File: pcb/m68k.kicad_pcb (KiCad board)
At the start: 2 copper layers, 100 x 100 mm, 120 parts, among them J1 USB_B_Micro, J2 Mini-DIN-6, J4 DB15_Male_HighDensity, J5 FTSH-105-01-L-DV-K, J6 FTSH-105-01-L-DV-K, J7 FTSH-105-01-L-DV-K, J8 Micro_SD_Card, U1 93LC56, U10 25LCxxx, U11 TXB0108DQSR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

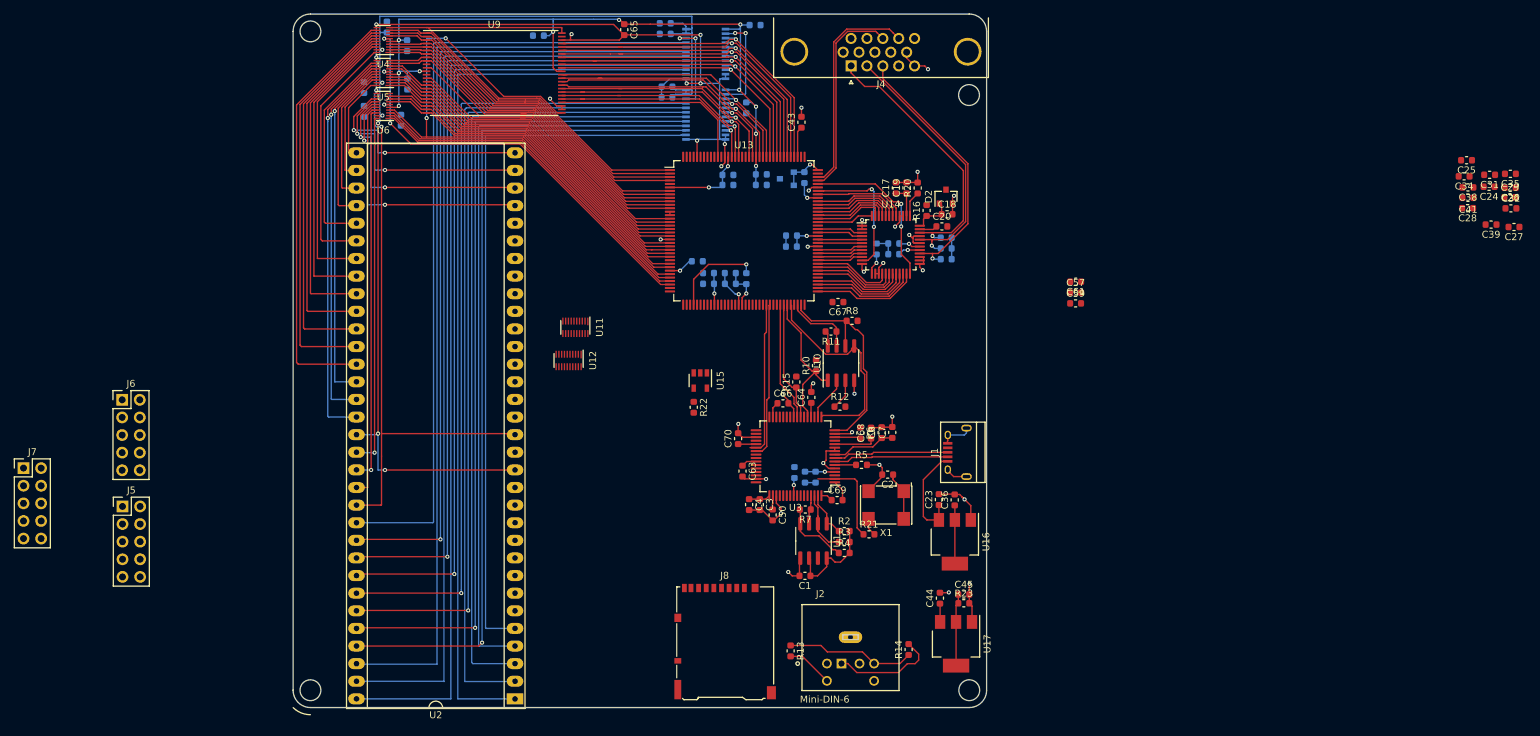
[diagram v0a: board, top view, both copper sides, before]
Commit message: Cleaned up CAPS
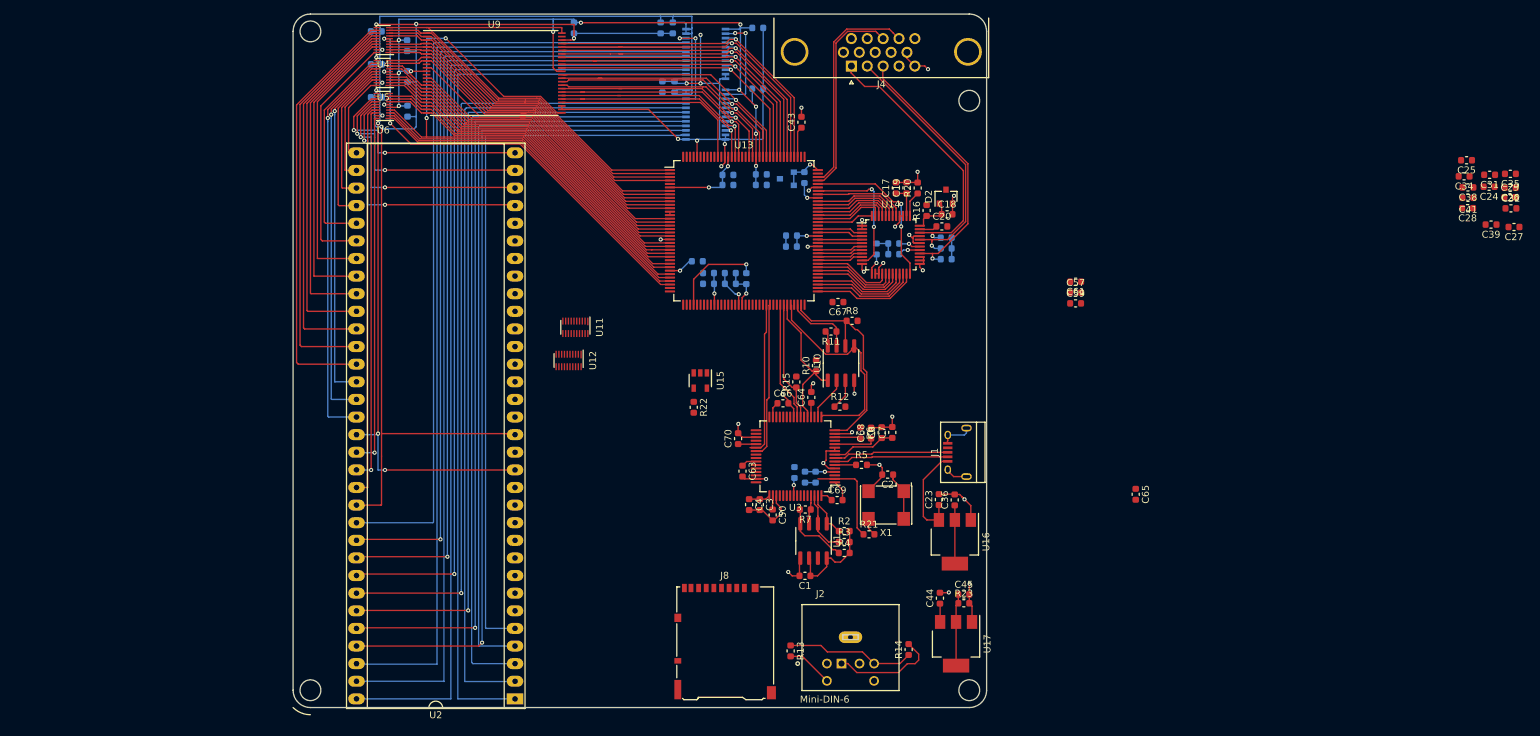
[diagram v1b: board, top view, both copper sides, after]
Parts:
- removed J5, J6, J7: FTSH-105-01-L-DV-K, Connector_PinHeader_2.54mm:PinHeader_2x05_P2.54mm_Vertical
- moved C65 99.6 mm to (141.5, 89.2)
- moved C54 5.25 mm to (60.5, 22.0), turned to 270 degrees
- moved C49 3.79 mm to (32.0, 27.2), turned to 180 degrees
- moved C60 3.23 mm to (87.0, 30.8), turned to 0 degrees
- moved C55 2.70 mm to (32.0, 32.0), turned to 180 degrees
- moved C42 1.65 mm to (32.0, 22.5), turned to 180 degrees
- moved C53 1.64 mm to (73.2, 30.5), turned to 90 degrees
- moved C52 1.61 mm to (36.5, 34.0)
- moved C46 1.39 mm to (74.8, 22.0), turned to 270 degrees
- moved C16 1.10 mm to (36.5, 29.0)
- moved C51 1.09 mm to (75.0, 30.5), turned to 90 degrees
- moved C47 0.94 mm to (73.0, 22.0), turned to 270 degrees
- moved C56 0.56 mm to (87.0, 22.0)
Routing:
- net GND: track 312.1 -> 367.0 mm, vias 38 -> 39
- net +5V: track 196.5 -> 199.8 mm
- net +3V3: track 217.8 -> 218.4 mm
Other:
- outline, holes or cut-outs redrawn

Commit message: Repin
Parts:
- moved U11 13.5 mm to (59.5, 51.8), turned to 180 degrees
- moved U12 12.3 mm to (59.9, 57.6), turned to 180 degrees
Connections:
- U13 pad 107: DIR -> BERRn
- U13 pad 110: BERRn -> DIR
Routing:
- net DIR: track 14.6 -> 26.3 mm, vias 2 -> 3
- net GND: track 367.0 -> 375.1 mm
- net +3V3: track 218.4 -> 217.0 mm

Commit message: SRAM!!!!
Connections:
- U13 pad 135: Net-(U11-Pad4) -> DATA_OEn
- U13 pad 136: Net-(U11-Pad7) -> Net-(U11-Pad4)
- U13 pad 137: Net-(U11-Pad8) -> Net-(U11-Pad7)
- U13 pad 138: Net-(U12-Pad1) -> Net-(U11-Pad8)
- U13 pad 139: Net-(U12-Pad2) -> Net-(U12-Pad1)
- U13 pad 141: Net-(U12-Pad3) -> Net-(U12-Pad2)
- U13 pad 142: Net-(U12-Pad4) -> Net-(U12-Pad3)
- U13 pad 143: Net-(U12-Pad7) -> Net-(U12-Pad4)
- U13 pad 144: Net-(U13-Pad144) -> /CE#
- U13 pad 60: DATA_OEn -> Net-(U12-Pad7)
- U9 pad 26: GND -> /CE#
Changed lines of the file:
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@@
   (net 241 "Net-(J2-Pad2)")
   (net 242 "Net-(U13-Pad134)")
-  (net 243 "Net-(U13-Pad144)")
-  (net 244 ADBUS)
+  (net 243 ADBUS)
+  (net 244 /CE#)
   (net_class Default "This is the default net class."
     (clearance 0.127)
@@
     (add_net /A8)
     (add_net /A9)
+    (add_net /CE#)
     (add_net /D0)
     (add_net /D1)
@@
     (add_net "Net-(U13-Pad133)")
     (add_net "Net-(U13-Pad134)")
-    (add_net "Net-(U13-Pad144)")
     (add_net "Net-(U13-Pad35)")
     (add_net "Net-(U13-Pad36)")
@@
       (net 1 GND))
     (pad 60 smd roundrect (at 2.75 10.6625) (size 0.3 1.475) (layers F.Cu F.Paste F.Mask) (roundrect_rratio 0.25)
-      (net 130 DATA_OEn))
+      (net 148 "Net-(U12-Pad7)"))
     (pad 61 smd roundrect (at 3.25 10.6625) (size 0.3 1.475) (layers F.Cu F.Paste F.Mask) (roundrect_rratio 0.25)
       (net 94 RX))
@@
       (net 26 nWP))
     (pad 64 smd roundrect (at 4.75 10.6625) (size 0.3 1.475) (layers F.Cu F.Paste F.Mask) (roundrect_rratio 0.25)
-      (net 244 ADBUS))
+      (net 243 ADBUS))
     (pad 65 smd roundrect (at 5.25 10.6625) (size 0.3 1.475) (layers F.Cu F.Paste F.Mask) (roundrect_rratio 0.25)
       (net 95 CDONE))
@@
       (net 242 "Net-(U13-Pad134)"))
     (pad 135 smd roundrect (at -4.25 -10.6625) (size 0.3 1.475) (layers F.Cu F.Paste F.Mask) (roundrect_rratio 0.25)
-      (net 144 "Net-(U11-Pad4)"))
+      (net 130 DATA_OEn))
     (pad 136 smd roundrect (at -4.75 -10.6625) (size 0.3 1.475) (layers F.Cu F.Paste F.Mask) (roundrect_rratio 0.25)
-      (net 143 "Net-(U11-Pad7)"))
+      (net 144 "Net-(U11-Pad4)"))
     (pad 137 smd roundrect (at -5.25 -10.6625) (size 0.3 1.475) (layers F.Cu F.Paste F.Mask) (roundrect_rratio 0.25)
-      (net 142 "Net-(U11-Pad8)"))
+      (net 143 "Net-(U11-Pad7)"))
     (pad 138 smd roundrect (at -5.75 -10.6625) (size 0.3 1.475) (layers F.Cu F.Paste F.Mask) (roundrect_rratio 0.25)
-      (net 145 "Net-(U12-Pad1)"))
+      (net 142 "Net-(U11-Pad8)"))
     (pad 139 smd roundrect (at -6.25 -10.6625) (size 0.3 1.475) (layers F.Cu F.Paste F.Mask) (roundrect_rratio 0.25)
-      (net 146 "Net-(U12-Pad2)"))
+      (net 145 "Net-(U12-Pad1)"))
     (pad 140 smd roundrect (at -6.75 -10.6625) (size 0.3 1.475) (layers F.Cu F.Paste F.Mask) (roundrect_rratio 0.25)
       (net 1 GND))
     (pad 141 smd roundrect (at -7.25 -10.6625) (size 0.3 1.475) (layers F.Cu F.Paste F.Mask) (roundrect_rratio 0.25)
-      (net 147 "Net-(U12-Pad3)"))
+      (net 146 "Net-(U12-Pad2)"))
     (pad 142 smd roundrect (at -7.75 -10.6625) (size 0.3 1.475) (layers F.Cu F.Paste F.Mask) (roundrect_rratio 0.25)
-      (net 179 "Net-(U12-Pad4)"))
+      (net 147 "Net-(U12-Pad3)"))
     (pad 143 smd roundrect (at -8.25 -10.6625) (size 0.3 1.475) (layers F.Cu F.Paste F.Mask) (roundrect_rratio 0.25)
-      (net 148 "Net-(U12-Pad7)"))
+      (net 179 "Net-(U12-Pad4)"))
     (pad 144 smd roundrect (at -8.75 -10.6625) (size 0.3 1.475) (layers F.Cu F.Paste F.Mask) (roundrect_rratio 0.25)
-      (net 243 "Net-(U13-Pad144)"))
+      (net 244 /CE#))
     (model ${KISYS3DMOD}/Package_QFP.3dshapes/TQFP-144_20x20mm_P0.5mm.wrl
       (at (xyz 0 0 0))
@@
       (net 96 "Net-(U10-Pad5)"))
     (pad 18 smd roundrect (at -3.25 5.675 180) (size 0.3 1.55) (layers F.Cu F.Paste F.Mask) (roundrect_rratio 0.25)
-      (net 244 ADBUS))
+      (net 243 ADBUS))
     (pad 19 smd roundrect (at -2.75 5.675 180) (size 0.3 1.55) (layers F.Cu F.Paste F.Mask) (roundrect_rratio 0.25)
       (net 197 "Net-(U3-Pad19)"))
@@
       (net 1 GND))
     (pad 26 smd rect (at 9.75 5.25) (size 1.1 0.25) (layers F.Cu F.Paste F.Mask)
-      (net 1 GND))
+      (net 244 /CE#))
     (pad 24 smd rect (at -9.75 5.75) (size 1.1 0.25) (layers F.Cu F.Paste F.Mask)
       (net 98 /a2))
@@
       (net 26 nWP))
     (pad 2 smd roundrect (at -2.475 -0.635 90) (size 1.95 0.6) (layers F.Cu F.Paste F.Mask) (roundrect_rratio 0.25)
-      (net 244 ADBUS))
+      (net 243 ADBUS))
     (pad 1 smd roundrect (at -2.475 -1.905 90) (size 1.95 0.6) (layers F.Cu F.Paste F.Mask) (roundrect_rratio 0.25)
       (net 24 "Net-(R10-Pad1)"))
@@
   (segment (start 81.25 35.266275) (end 81.25 40.5875) (width 0.127) (layer F.Cu) (net 242))
   (segment (start 78.733725 32.75) (end 81.25 35.266275) (width 0.127) (layer F.Cu) (net 242))
-  (segment (start 95.68 77.433674) (end 95.6862 77.427474) (width 0.2) (layer F.Cu) (net 244))
-  (segment (start 95.68 78.0976) (end 95.68 77.433674) (width 0.2) (layer F.Cu) (net 244))
-  (segment (start 95.6862 77.427474) (end 95.6862 76.74) (width 0.2) (layer F.Cu) (net 244))
-  (segment (start 98.3659 74.0603) (end 98.3659 72.8142) (width 0.2) (layer F.Cu) (net 244))
-  (segment (start 95.6862 76.74) (end 98.3659 74.0603) (width 0.2) (layer F.Cu) (net 244))
+  (segment (start 95.68 77.433674) (end 95.6862 77.427474) (width 0.2) (layer F.Cu) (net 243))
+  (segment (start 95.68 78.0976) (end 95.68 77.433674) (width 0.2) (layer F.Cu) (net 243))
+  (segment (start 95.6862 77.427474) (end 95.6862 76.74) (width 0.2) (layer F.Cu) (net 243))
+  (segment (start 98.3659 74.0603) (end 98.3659 72.8142) (width 0.2) (layer F.Cu) (net 243))
+  (segment (start 95.6862 76.74) (end 98.3659 74.0603) (width 0.2) (layer F.Cu) (net 243))
 )

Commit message: SRAM????
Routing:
- net +5V: track 199.8 -> 232.3 mm
- net /CE#: track 0.00 -> 21.0 mm
- net GND: track 375.1 -> 393.1 mm
- net DATA_OEn: track 13.3 -> 22.8 mm, vias 2 -> 3
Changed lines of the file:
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@@
     (thickness 1.6)
     (drawings 13)
-    (tracks 1583)
+    (tracks 1597)
     (zones 0)
     (modules 117)
@@
   (segment (start 115.0875 47.3299) (end 115.0922 47.3252) (width 0.2) (layer F.Cu) (net 1))
   (segment (start 115.0875 48.875) (end 115.0875 47.3299) (width 0.2) (layer F.Cu) (net 1))
-  (segment (start 58.75 33.25) (end 58.75 33.75) (width 0.2) (layer F.Cu) (net 1))
   (segment (start 32.1 31.1) (end 32 31) (width 0.2) (layer F.Cu) (net 1))
   (via (at 32 31) (size 0.6) (drill 0.3) (layers F.Cu B.Cu) (net 1))
@@
   (via (at 75.5 38) (size 0.6) (drill 0.3) (layers F.Cu B.Cu) (net 1))
   (segment (start 71.25 33.75) (end 75.5 38) (width 0.2) (layer F.Cu) (net 1))
-  (segment (start 58.75 33.75) (end 71.25 33.75) (width 0.2) (layer F.Cu) (net 1))
   (segment (start 75.575 38.075) (end 75.5 38) (width 0.2) (layer B.Cu) (net 1))
   (segment (start 76.65 38.075) (end 75.575 38.075) (width 0.2) (layer B.Cu) (net 1))
@@
   (segment (start 60.5 23.5) (end 60.5 22.7875) (width 0.2) (layer B.Cu) (net 1))
   (segment (start 37.75 21.5) (end 60.5 21.5) (width 0.2) (layer F.Cu) (net 1))
-  (segment (start 60.5 21.5) (end 60.5 23.5) (width 0.2) (layer F.Cu) (net 1))
   (segment (start 60.5 22.7875) (end 73 22.7875) (width 0.2) (layer B.Cu) (net 1))
   (segment (start 74.75 22.7875) (end 73 22.7875) (width 0.2) (layer B.Cu) (net 1))
@@
   (segment (start 93.3 33.5) (end 93.3 30.8) (width 0.2) (layer F.Cu) (net 1))
   (segment (start 93.25 30.75) (end 87.7875 30.75) (width 0.2) (layer B.Cu) (net 1))
+  (segment (start 70.75 33.25) (end 71.25 33.75) (width 0.2) (layer F.Cu) (net 1))
+  (segment (start 58.75 33.25) (end 70.75 33.25) (width 0.2) (layer F.Cu) (net 1))
+  (segment (start 60.5 22.75) (end 78.5 22.75) (width 0.2) (layer F.Cu) (net 1))
+  (segment (start 60.5 21.5) (end 60.5 22.75) (width 0.2) (layer F.Cu) (net 1))
+  (segment (start 60.5 22.75) (end 60.5 23.5) (width 0.2) (layer F.Cu) (net 1))
+  (segment (start 78.5 22.75) (end 78.75 23) (width 0.2) (layer F.Cu) (net 1))
   (segment (start 115.424 90.8742) (end 115.399 90.8492) (width 0.2) (layer F.Cu) (net 2))
   (segment (start 115.424 92.9492) (end 115.424 90.8742) (width 0.2) (layer F.Cu) (net 2))
@@
   (segment (start 76.65 30.925) (end 75.3625 30.925) (width 0.2) (layer B.Cu) (net 8))
   (segment (start 75 31.2875) (end 73.25 31.2875) (width 0.2) (layer B.Cu) (net 8))
+  (segment (start 77.5 20.32501) (end 103.82501 20.32501) (width 0.2) (layer B.Cu) (net 8))
+  (segment (start 106.225 22.725) (end 106.225 25.52) (width 0.2) (layer B.Cu) (net 8))
+  (segment (start 103.82501 20.32501) (end 106.225 22.725) (width 0.2) (layer B.Cu) (net 8))
   (segment (start 115.597 105.2909) (end 115.9245 104.9634) (width 0.2) (layer F.Cu) (net 9))
   (segment (start 115.597 107.6574) (end 115.597 105.2909) (width 0.2) (layer F.Cu) (net 9))
@@
   (segment (start 78.025 32.225) (end 76.65 32.225) (width 0.127) (layer B.Cu) (net 130))
   (segment (start 78.027 32.223) (end 78.025 32.225) (width 0.127) (layer B.Cu) (net 130))
+  (via (at 80.7595 35.5) (size 0.6) (drill 0.3) (layers F.Cu B.Cu) (net 130))
+  (segment (start 78.027 32.7675) (end 80.7595 35.5) (width 0.127) (layer B.Cu) (net 130))
+  (segment (start 78.027 32.223) (end 78.027 32.7675) (width 0.127) (layer B.Cu) (net 130))
+  (segment (start 80.7595 40.578) (end 80.75 40.5875) (width 0.127) (layer F.Cu) (net 130))
+  (segment (start 80.7595 35.5) (end 80.7595 40.578) (width 0.127) (layer F.Cu) (net 130))
   (via (at 83.844398 23.648) (size 0.6) (drill 0.3) (layers F.Cu B.Cu) (net 131))
   (segment (start 92.25 32.053602) (end 83.844398 23.648) (width 0.127) (layer F.Cu) (net 131))
@@
   (segment (start 98.3659 74.0603) (end 98.3659 72.8142) (width 0.2) (layer F.Cu) (net 243))
   (segment (start 95.6862 76.74) (end 98.3659 74.0603) (width 0.2) (layer F.Cu) (net 243))
+  (segment (start 76.25 39.529962) (end 76.25 40.5875) (width 0.2) (layer F.Cu) (net 244))
+  (segment (start 70.470038 33.75) (end 76.25 39.529962) (width 0.2) (layer F.Cu) (net 244))
+  (segment (start 58.75 33.75) (end 70.470038 33.75) (width 0.2) (layer F.Cu) (net 244))
 )

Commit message: SAVE
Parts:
- moved U11 8.53 mm to (64.0, 59.0)
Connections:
- U11 pad 13: Net-(U11-Pad13) -> ASn
- U11 pad 14: FC2 -> E
- U11 pad 15: FC1 -> VMAn
- U11 pad 16: FC0 -> BGn
- U11 pad 17: LDSn -> FC2
- U11 pad 18: UDSn -> FC1
- U11 pad 20: R_Wn -> FC0
- U12 pad 10: PS2_CLK -> Net-(U12-Pad10)
- U12 pad 12: Net-(J2-Pad5) -> Net-(U12-Pad12)
- U12 pad 13: Net-(J2-Pad1) -> LDSn
- U12 pad 14: RESETn -> UDSn
- U12 pad 15: HALTn -> R_Wn
- U12 pad 16: ASn -> Net-(J2-Pad5)
- U12 pad 17: E -> Net-(J2-Pad1)
- U12 pad 18: VMAn -> RESETn
- U12 pad 2: Net-(U12-Pad2) -> CDONE
- U12 pad 20: BGn -> HALTn
- U12 pad 3: Net-(U12-Pad3) -> PS2_DATA
- U12 pad 4: Net-(U12-Pad4) -> PS2_CLK
- U12 pad 8: CDONE -> Net-(U12-Pad8)
- U12 pad 9: PS2_DATA -> Net-(U12-Pad9)
- U13 pad 136: Net-(U11-Pad4) -> Net-(U11-Pad1)
- U13 pad 137: Net-(U11-Pad7) -> Net-(U11-Pad2)
- U13 pad 138: Net-(U11-Pad8) -> Net-(U11-Pad3)
- U13 pad 139: Net-(U12-Pad1) -> Net-(U11-Pad4)
- U13 pad 141: Net-(U12-Pad2) -> Net-(U11-Pad7)
- U13 pad 142: Net-(U12-Pad3) -> Net-(U11-Pad8)
- U13 pad 143: Net-(U12-Pad4) -> Net-(U11-Pad9)
- U13 pad 15: Net-(U11-Pad1) -> Net-(U12-Pad7)
- U13 pad 16: Net-(U11-Pad2) -> Net-(U12-Pad8)
- U13 pad 17: Net-(U11-Pad3) -> Net-(U12-Pad9)
- U13 pad 60: Net-(U12-Pad7) -> Net-(U12-Pad1)
- U9 pad 11: Net-(U11-Pad1) -> Net-(U12-Pad7)
- U9 pad 14: Net-(U11-Pad2) -> Net-(U12-Pad8)
- U9 pad 15: Net-(U11-Pad3) -> Net-(U12-Pad9)
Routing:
- net Net-(U12-Pad7): track 0.00 -> 44.8 mm
- net Net-(U11-Pad1): track 44.8 -> 0.00 mm
- net Net-(U12-Pad8): track 0.00 -> 44.4 mm
- net Net-(U11-Pad2): track 44.4 -> 0.00 mm
- net Net-(U12-Pad9): track 0.00 -> 43.7 mm
- net Net-(U11-Pad3): track 43.7 -> 0.00 mm
- net clk12: track 15.2 -> 13.8 mm, vias 1 -> 0

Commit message: Home
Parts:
- moved U12 13.3 mm to (71.2, 64.5), turned to 270 degrees
- moved U11 5.85 mm to (66.0, 64.5), turned to 270 degrees
- moved C10 4.72 mm to (87.0, 56.4)
- moved C15 4.72 mm to (83.9, 54.9)
- moved C33 4.72 mm to (83.9, 56.4)
- moved C58 4.72 mm to (82.3, 53.1)
- moved C9 4.72 mm to (87.0, 54.9)
- moved R9 4.72 mm to (89.3, 55.6)
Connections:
- U12 pad 1: Net-(U12-Pad1) -> CDONE
- U12 pad 18: RESETn -> HALTn
- U12 pad 2: CDONE -> Net-(U12-Pad2)
- U12 pad 20: HALTn -> RESETn
- U13 pad 60: Net-(U12-Pad1) -> Net-(U12-Pad2)
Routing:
- net CDONE: track 17.2 -> 38.4 mm, vias 0 -> 2
- net Net-(U12-Pad2): track 0.00 -> 18.8 mm, vias 0 -> 2
- net PS2_CLK: track 0.00 -> 17.5 mm, vias 0 -> 2
- net PS2_DATA: track 0.00 -> 17.4 mm, vias 0 -> 2
- net +1V2: track 28.2 -> 24.6 mm
- net +3V3: track 217.0 -> 213.9 mm
- net Net-(C10-Pad1): track 6.30 -> 4.44 mm
- net Net-(C10-Pad2): track 5.67 -> 4.16 mm

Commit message: I finally broke something
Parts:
- moved C27 123.2 mm to (74.0, 67.5), turned to 270 degrees
- moved C24 118.9 mm to (75.8, 67.5), turned to 270 degrees
- moved C65 76.2 mm to (68.5, 67.5)
- moved C57 56.8 mm to (189.6, 56.9)
- moved C59 56.8 mm to (189.6, 58.5)
- moved C61 56.8 mm to (189.6, 55.3), turned to 270 degrees
- moved U11 0.25 mm to (65.8, 64.5)
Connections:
- U11 pad 12: Net-(U11-Pad12) -> VMAn
- U11 pad 13: ASn -> BGn
- U11 pad 14: E -> FC2
- U11 pad 15: VMAn -> FC1
- U11 pad 16: BGn -> FC0
- U11 pad 17: FC2 -> LDSn
- U11 pad 18: FC1 -> UDSn
- U11 pad 20: FC0 -> R_Wn
- U12 pad 12: Net-(U12-Pad12) -> ASn
- U12 pad 13: LDSn -> E
- U12 pad 14: UDSn -> Net-(U12-Pad14)
- U12 pad 15: R_Wn -> Net-(U12-Pad15)
- U13 pad 136: Net-(U11-Pad1) -> Net-(U12-Pad9)
- U13 pad 137: Net-(U11-Pad2) -> Net-(U12-Pad10)
- U13 pad 138: Net-(U11-Pad3) -> Net-(U11-Pad4)
- U13 pad 139: Net-(U11-Pad4) -> Net-(U11-Pad7)
- U13 pad 141: Net-(U11-Pad7) -> Net-(U11-Pad8)
- U13 pad 142: Net-(U11-Pad8) -> Net-(U11-Pad9)
- U13 pad 143: Net-(U11-Pad9) -> Net-(U11-Pad10)
- U13 pad 15: Net-(U12-Pad7) -> Net-(U11-Pad1)
- U13 pad 16: Net-(U12-Pad8) -> Net-(U11-Pad2)
- U13 pad 17: Net-(U12-Pad9) -> Net-(U11-Pad3)
- U9 pad 11: Net-(U12-Pad7) -> Net-(U11-Pad1)
- U9 pad 14: Net-(U12-Pad8) -> Net-(U11-Pad2)
- U9 pad 15: Net-(U12-Pad9) -> Net-(U11-Pad3)
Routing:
- net Net-(U11-Pad1): track 0.00 -> 69.0 mm
- net Net-(U11-Pad2): track 0.00 -> 68.0 mm
- net Net-(U11-Pad3): track 0.00 -> 66.5 mm
- net Net-(U12-Pad7): track 44.8 -> 0.00 mm
- net Net-(U12-Pad8): track 44.4 -> 0.00 mm
- net Net-(U11-Pad7): track 0.00 -> 28.7 mm, vias 0 -> 2
- net Net-(U11-Pad10): track 0.00 -> 28.5 mm, vias 0 -> 2
- net Net-(U11-Pad8): track 0.00 -> 28.4 mm, vias 0 -> 2
- net Net-(U11-Pad9): track 0.00 -> 28.4 mm, vias 0 -> 2
- net Net-(U11-Pad4): track 0.00 -> 28.3 mm, vias 0 -> 2
- net Net-(U12-Pad10): track 0.00 -> 27.4 mm, vias 0 -> 2
- net +3V3: track 213.9 -> 234.4 mm
- net Net-(U12-Pad9): track 43.7 -> 27.3 mm, vias 0 -> 2
- net ADDR_OE: track 67.1 -> 78.3 mm, vias 4 -> 6

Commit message: Fin
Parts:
- moved R22 6.50 mm to (84.3, 76.5)
- moved U15 6.50 mm to (85.2, 72.6)
- moved C9 3.49 mm to (84.5, 57.2)
- moved C10 3.47 mm to (84.5, 58.8)
- moved C15 3.09 mm to (80.9, 54.1)
- moved C33 3.09 mm to (80.9, 55.6)
- moved C58 3.09 mm to (79.3, 52.4)
- moved R9 2.99 mm to (87.5, 58.0), turned to 0 degrees
- moved C14 0.53 mm to (87.0, 44.5)
- moved C12 0.52 mm to (87.0, 43.0)
- moved C11 0.28 mm to (82.5, 43.0), turned to 180 degrees
- moved R1 0.28 mm to (93.5, 43.8)
- moved C13 0.25 mm to (82.5, 44.5), turned to 180 degrees
- moved U18 0.20 mm to (91.0, 43.8)
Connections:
- U11 pad 12: VMAn -> FC0
- U11 pad 13: BGn -> FC1
- U11 pad 15: FC1 -> VMAn
- U11 pad 16: FC0 -> BGn
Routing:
- net GND: track 393.1 -> 451.5 mm, vias 39 -> 44
- net BERRn: track 0.00 -> 56.5 mm, vias 0 -> 3
- net +5V: track 232.3 -> 285.4 mm, vias 6 -> 8
- net BGACKn: track 0.00 -> 48.7 mm, vias 0 -> 4
- net ASn: track 0.00 -> 48.3 mm
- net BRn: track 0.00 -> 44.5 mm, vias 0 -> 2
- net UDSn: track 0.00 -> 44.5 mm
- net DTACKn: track 0.00 -> 44.3 mm, vias 0 -> 1
- net LDSn: track 0.00 -> 42.3 mm
- net R_Wn: track 0.00 -> 40.7 mm, vias 0 -> 1
- net VPAn: track 0.00 -> 36.3 mm, vias 0 -> 3
- net BGn: track 0.00 -> 34.4 mm, vias 0 -> 1
- net CLK68000: track 0.00 -> 32.0 mm, vias 0 -> 1
- net +3V3: track 234.4 -> 264.0 mm, vias 22 -> 24
- net HALTn: track 0.00 -> 29.1 mm, vias 0 -> 1
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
